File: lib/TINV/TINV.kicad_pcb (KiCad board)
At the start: 2 copper layers, 4 parts

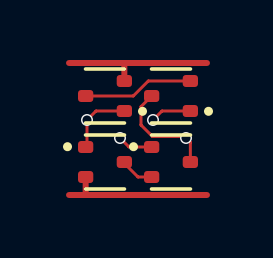
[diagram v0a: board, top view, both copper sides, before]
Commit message: All cells now use 1mm*4mm grid rather than 1.1mm*4.4mm
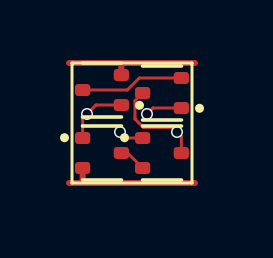
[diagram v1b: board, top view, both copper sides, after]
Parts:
- moved N2 0.42 mm to (3.00, 3.00)
- moved N1 0.32 mm to (1.00, 3.00)
- moved P2 0.32 mm to (3.00, 1.00)
- moved P1 0.22 mm to (1.00, 0.90)
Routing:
- net VDD: track 5.22 -> 4.62 mm
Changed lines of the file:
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@@
 	(footprint "Package_TO_SOT_SMD:SOT-523"
 		(layer "F.Cu")
-		(at 3.3 3.3)
+		(at 3 3)
 		(descr "SOT523, https://www.diodes.com/assets/Package-Files/SOT523.pdf")
 		(tags "SOT-523")
@@
 	(footprint "Package_TO_SOT_SMD:SOT-523"
 		(layer "F.Cu")
-		(at 3.3 1.1 180)
+		(at 3 1 180)
 		(descr "SOT523, https://www.diodes.com/assets/Package-Files/SOT523.pdf")
 		(tags "SOT-523")
@@
 	(footprint "Package_TO_SOT_SMD:SOT-523"
 		(layer "F.Cu")
-		(at 1.1 3.3)
+		(at 1 3)
 		(descr "SOT523, https://www.diodes.com/assets/Package-Files/SOT523.pdf")
 		(tags "SOT-523")
@@
 	(footprint "Package_TO_SOT_SMD:SOT-523"
 		(layer "F.Cu")
-		(at 1.1 1.1 180)
+		(at 1 0.9 180)
 		(descr "SOT523, https://www.diodes.com/assets/Package-Files/SOT523.pdf")
 		(tags "SOT-523")
@@
 		)
 	)
-	(segment
-		(start 2.299 1.456)
-		(end 2.299 2.0661)
+	(gr_rect
+		(start 0 0)
+		(end 4 4)
+		(stroke
+			(width 0.1)
+			(type default)
+		)
+		(fill no)
+		(layer "F.SilkS")
+	)
+	(segment
+		(start 3.349 2.149)
+		(end 3.5 2.3)
 		(width 0.1)
 		(layer "F.Cu")
@@
 	)
 	(segment
-		(start 2.299 2.0661)
-		(end 2.6819 2.449)
+		(start 3.645 3)
+		(end 3.645 2.445)
 		(width 0.1)
 		(layer "F.Cu")
@@
 	)
 	(segment
-		(start 3.945 3.3)
-		(end 3.945 2.645)
+		(start 3.645 2.445)
+		(end 3.5 2.3)
 		(width 0.1)
 		(layer "F.Cu")
@@
 	)
 	(segment
-		(start 2.655 1.1)
-		(end 2.299 1.456)
+		(start 2.355 1)
+		(end 2.099 1.256)
 		(width 0.1)
 		(layer "F.Cu")
@@
 	)
 	(segment
-		(start 3.945 2.645)
-		(end 3.8 2.5)
+		(start 2.3819 2.149)
+		(end 3.349 2.149)
 		(width 0.1)
 		(layer "F.Cu")
@@
 	)
 	(segment
-		(start 3.749 2.449)
-		(end 3.8 2.5)
+		(start 2.099 1.256)
+		(end 2.099 1.8661)
 		(width 0.1)
 		(layer "F.Cu")
@@
 	)
 	(segment
-		(start 2.6819 2.449)
-		(end 3.749 2.449)
+		(start 2.099 1.8661)
+		(end 2.3819 2.149)
 		(width 0.1)
 		(layer "F.Cu")
@@
 	)
 	(via
-		(at 3.8 2.5)
+		(at 3.5 2.3)
 		(size 0.4)
 		(drill 0.3)
@@
 	)
 	(segment
-		(start 0.455 3.8)
-		(end 0.455 4.395)
+		(start 0.3 4)
+		(end -0.1 4)
 		(width 0.2)
 		(layer "F.Cu")
@@
 	)
 	(segment
-		(start 0.455 4.395)
-		(end 0.45 4.4)
+		(start 0.455 4)
+		(end 0.45 4)
 		(width 0.2)
 		(layer "F.Cu")
@@
 	)
 	(segment
-		(start 0.45 4.4)
-		(end -0.1 4.4)
+		(start 0.45 4)
+		(end 0.3 4)
 		(width 0.2)
 		(layer "F.Cu")
@@
 	)
 	(segment
-		(start 4.5 4.4)
-		(end 0.45 4.4)
+		(start 4.1 4)
+		(end 0.45 4)
 		(width 0.2)
 		(layer "F.Cu")
@@
 	)
 	(segment
-		(start 0.8 1.6)
-		(end 1.745 1.6)
+		(start 0.355 3.5)
+		(end 0.355 3.945)
+		(width 0.2)
+		(layer "F.Cu")
+		(net 2)
+	)
+	(segment
+		(start 0.355 3.945)
+		(end 0.3 4)
+		(width 0.2)
+		(layer "F.Cu")
+		(net 2)
+	)
+	(segment
+		(start 0.355 1.845)
+		(end 0.5 1.7)
 		(width 0.1)
 		(layer "F.Cu")
@@
 	)
 	(segment
-		(start 0.5 2.755)
-		(end 0.455 2.8)
+		(start 1.645 1.4)
+		(end 0.8 1.4)
 		(width 0.1)
 		(layer "F.Cu")
@@
 	)
 	(segment
-		(start 0.5 1.9)
-		(end 0.5 2.755)
+		(start 0.355 2.5)
+		(end 0.355 1.845)
 		(width 0.1)
 		(layer "F.Cu")
@@
 	)
 	(segment
-		(start 0.5 1.9)
-		(end 0.8 1.6)
+		(start 0.8 1.4)
+		(end 0.5 1.7)
 		(width 0.1)
 		(layer "F.Cu")
@@
 	)
 	(via
-		(at 0.5 1.9)
+		(at 0.5 1.7)
 		(size 0.4)
 		(drill 0.3)
@@
 	)
 	(segment
-		(start 1.745 0.6)
-		(end 1.745 0.045)
+		(start 1.645 0.4)
+		(end 1.645 0.045)
 		(width 0.2)
 		(layer "F.Cu")
@@
 	(segment
 		(start 1.7 0)
+		(end 1.6 0)
+		(width 0.2)
+		(layer "F.Cu")
+		(net 4)
+	)
+	(segment
+		(start 1.645 0.045)
+		(end 1.6 0)
+		(width 0.2)
+		(layer "F.Cu")
+		(net 4)
+	)
+	(segment
+		(start 1.6 0)
 		(end -0.1 0)
 		(width 0.2)
@@
 	)
 	(segment
-		(start 4.5 0)
-		(end 3.95 0)
-		(width 0.2)
-		(layer "F.Cu")
-		(net 4)
-	)
-	(segment
-		(start 3.95 0)
+		(start 4.1 0)
 		(end 1.7 0)
 		(width 0.2)
@@
 	)
 	(segment
-		(start 1.745 0.045)
-		(end 1.7 0)
-		(width 0.2)
-		(layer "F.Cu")
-		(net 4)
-	)
-	(segment
-		(start 2.2 3.8)
-		(end 2.655 3.8)
+		(start 1.645 3)
+		(end 1.855 3)
 		(width 0.1)
 		(layer "F.Cu")
@@
 	)
 	(segment
-		(start 1.745 3.345)
-		(end 2.2 3.8)
+		(start 1.855 3)
+		(end 2.355 3.5)
 		(width 0.1)
 		(layer "F.Cu")
@@
 	)
 	(segment
-		(start 1.745 3.3)
-		(end 1.745 3.345)
-		(width 0.2)
-		(layer "F.Cu")
-		(net 5)
-	)
-	(segment
-		(start 1.6 2.5)
-		(end 1.9 2.8)
+		(start 2.355 2.5)
+		(end 1.8 2.5)
 		(width 0.1)
 		(layer "F.Cu")
@@
 	)
 	(segment
-		(start 1.9 2.8)
-		(end 2.655 2.8)
+		(start 1.8 2.5)
+		(end 1.6 2.3)
 		(width 0.1)
 		(layer "F.Cu")
@@
 	)
 	(via
-		(at 1.6 2.5)
+		(at 1.6 2.3)
 		(size 0.4)
 		(drill 0.3)
@@
 	)
 	(segment
-		(start 2.042262 1.1)
-		(end 2.542262 0.6)
+		(start 0.355 0.9)
+		(end 1.842262 0.9)
 		(width 0.1)
 		(layer "F.Cu")
@@
 	)
 	(segment
-		(start 2.542262 0.6)
-		(end 3.945 0.6)
+		(start 1.842262 0.9)
+		(end 2.242262 0.5)
 		(width 0.1)
 		(layer "F.Cu")
@@
 	)
 	(segment
-		(start 0.455 1.1)
-		(end 2.042262 1.1)
+		(start 2.242262 0.5)
+		(end 3.645 0.5)
 		(width 0.1)
 		(layer "F.Cu")
@@
 	)
 	(segment
-		(start 3 1.6)
-		(end 2.7 1.9)
+		(start 3.645 1.5)
+		(end 2.7 1.5)
 		(width 0.1)
 		(layer "F.Cu")
@@
 	)
 	(segment
-		(start 3.945 1.6)
-		(end 3 1.6)
+		(start 2.7 1.5)
+		(end 2.5 1.7)
 		(width 0.1)
 		(layer "F.Cu")
@@
 	)
 	(via
-		(at 2.7 1.9)
+		(at 2.5 1.7)
 		(size 0.4)
 		(drill 0.3)

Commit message: Make the pads of my SOT523 footprint very slightly smaller, which is enough to route all the cells and leave the mosfets exactly on the grid
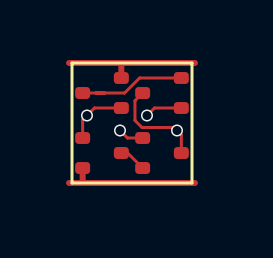
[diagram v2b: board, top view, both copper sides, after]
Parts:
- N1, N2, P1, P2: footprint Package_TO_SOT_SMD:SOT-523 -> RV523:SOT523
- moved P1 0.10 mm to (1.00, 1.00)

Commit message: Propagate MOSFET values to the cells' PCBs
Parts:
- N1, N2: value (none) -> NMOS
- P1, P2: value (none) -> PMOS
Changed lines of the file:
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@@
 			)
 		)
-		(property "Value" ""
+		(property "Value" "NMOS"
 			(at 0 0 0)
 			(layer "F.Fab")
@@
 			)
 		)
-		(property "Value" ""
+		(property "Value" "PMOS"
 			(at 0 0 180)
 			(layer "F.Fab")
@@
 			)
 		)
-		(property "Value" ""
+		(property "Value" "NMOS"
 			(at 0 0 0)
 			(layer "F.Fab")
@@
 			)
 		)
-		(property "Value" ""
+		(property "Value" "PMOS"
 			(at 0 0 180)
 			(layer "F.Fab")
